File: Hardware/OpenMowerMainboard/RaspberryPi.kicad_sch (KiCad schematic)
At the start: 13 parts, among them J21 Raspberry_Pi_2_3, J22 Conn_02x04_Odd_Even, M1 Fan, Q3 BSS138, SW1 MK-11C04-G013, U3 SIP32509DT

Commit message: feat(bom): update LCSC codes
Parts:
- J21: LCSC (none) -> C2685119
- Q3: LCSC C360338 -> C3040446
- R1, R2, R4: LCSC (none) -> C17414
- R5: LCSC (none) -> C114523
- U3: LCSC (none) -> C335619
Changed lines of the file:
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@@
+      (effects (font (size 1.27 1.27)) hide)
+    )
+    (property "LCSC" "C17414" (id 7) (at 184.15 152.4 0)
       (effects (font (size 1.27 1.27)) hide)
     )
@@
       (effects (font (size 1.27 1.27)) hide)
     )
+    (property "LCSC" "C335619" (id 7) (at 166.37 17.78 0)
+      (effects (font (size 1.27 1.27)) hide)
+    )
     (pin "1")
     (pin "2")
@@
       (effects (font (size 1.27 1.27)) hide)
     )
+    (property "LCSC" "C114523" (id 7) (at 101.6 49.53 0)
+      (effects (font (size 1.27 1.27)) hide)
+    )
     (pin "1")
     (pin "2")
@@
       (effects (font (size 1.27 1.27)) (justify left) hide)
     )
-    (property "LCSC" "C360338" (id 4) (at 114.3 49.53 0)
+    (property "LCSC" "C3040446" (id 4) (at 114.3 49.53 0)
       (effects (font (size 1.27 1.27)) hide)
     )
@@
       (effects (font (size 1.27 1.27)) hide)
     )
+    (property "LCSC" "C17414" (id 7) (at 93.98 57.15 0)
+      (effects (font (size 1.27 1.27)) hide)
+    )
     (pin "1")
     (pin "2")
@@
     )
     (property "Stock_PN" "J-SMD-2x20-.1F" (id 6) (at 107.315 133.985 0)
+      (effects (font (size 1.27 1.27)) hide)
+    )
+    (property "LCSC" "C2685119" (id 7) (at 107.315 133.985 0)
       (effects (font (size 1.27 1.27)) hide)
     )
@@
       (effects (font (size 1.27 1.27)) hide)
     )
+    (property "LCSC" "C17414" (id 7) (at 184.15 130.175 0)
+      (effects (font (size 1.27 1.27)) hide)
+    )

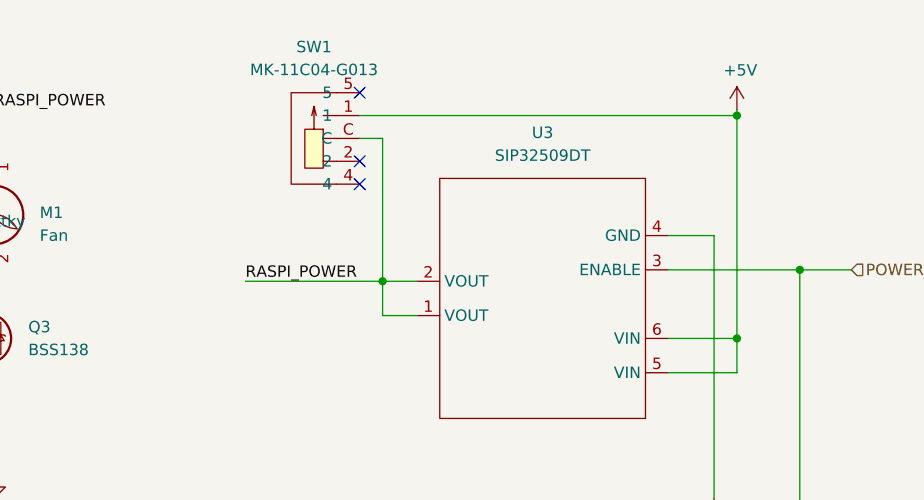
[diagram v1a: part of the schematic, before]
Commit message: feat(mb): add pin header for RPi force power
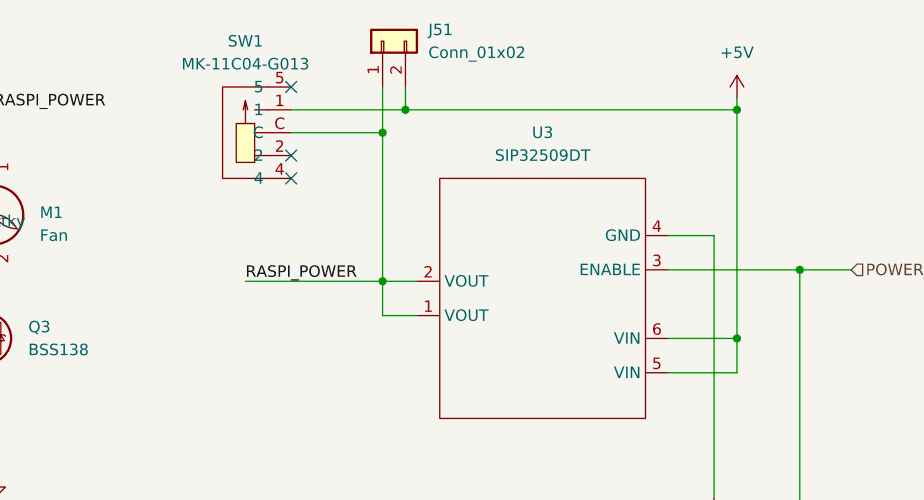
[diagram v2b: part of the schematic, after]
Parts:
- added J51: Conn_01x02, Connector_PinHeader_2.54mm:PinHeader_1x02_P2.54mm_Vertical, symbol Connector_Generic:Conn_01x02
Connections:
- net +5V: now also J51.2 (Pin_2)
- net RASPI_POWER: now also J51.1 (Pin_1)
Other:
- moved on the sheet: SW1
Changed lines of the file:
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@@
   (junction (at 107.315 171.45) (diameter 0) (color 0 0 0 0)
   )
+  (junction (at 162.56 24.13) (diameter 0) (color 0 0 0 0)
+  )
   (junction (at 114.935 171.45) (diameter 0) (color 0 0 0 0)
   )
@@
   (junction (at 116.84 43.18) (diameter 0) (color 0 0 0 0)
   )
-  (junction (at 199.39 24.765) (diameter 0) (color 0 0 0 0)
+  (junction (at 199.39 24.13) (diameter 0) (color 0 0 0 0)
   )
   (junction (at 102.235 171.45) (diameter 0) (color 0 0 0 0)
@@
   (junction (at 206.375 41.91) (diameter 0) (color 0 0 0 0)
   )
-  (no_connect (at 157.48 32.385))
-  (no_connect (at 157.48 29.845))
+  (junction (at 160.02 26.67) (diameter 0) (color 0 0 0 0)
+  )
+  (no_connect (at 149.86 31.75))
+  (no_connect (at 149.86 29.21))
   (no_connect (at 127.635 121.285))
   (no_connect (at 127.635 118.745))
@@
   (no_connect (at 127.635 146.685))
   (no_connect (at 127.635 136.525))
-  (no_connect (at 157.48 22.225))
+  (no_connect (at 149.86 21.59))
   (wire (pts (xy 158.115 111.125) (xy 127.635 111.125))
     (stroke (width 0) (type default) (color 0 0 0 0))
@@
     (stroke (width 0) (type default) (color 0 0 0 0))
   )
+  (wire (pts (xy 160.02 21.59) (xy 160.02 26.67))
+    (stroke (width 0) (type default) (color 0 0 0 0))
+  )
+  (wire (pts (xy 162.56 21.59) (xy 162.56 24.13))
+    (stroke (width 0) (type default) (color 0 0 0 0))
+  )
   (wire (pts (xy 127.635 144.145) (xy 184.15 144.145))
     (stroke (width 0) (type default) (color 0 0 0 0))
@@
     (stroke (width 0) (type default) (color 0 0 0 0))
   )
-  (wire (pts (xy 157.48 24.765) (xy 199.39 24.765))
+  (wire (pts (xy 149.86 24.13) (xy 162.56 24.13))
     (stroke (width 0) (type default) (color 0 0 0 0))
   )
@@
     (stroke (width 0) (type default) (color 0 0 0 0))
   )
-  (wire (pts (xy 157.48 27.305) (xy 160.02 27.305))
+  (wire (pts (xy 149.86 26.67) (xy 160.02 26.67))
     (stroke (width 0) (type default) (color 0 0 0 0))
   )
@@
     (stroke (width 0) (type default) (color 0 0 0 0))
   )
-  (wire (pts (xy 160.02 27.305) (xy 160.02 43.18))
-    (stroke (width 0) (type default) (color 0 0 0 0))
-  )
-  (wire (pts (xy 199.39 24.765) (xy 199.39 49.53))
+  (wire (pts (xy 199.39 24.13) (xy 199.39 49.53))
     (stroke (width 0) (type default) (color 0 0 0 0))
   )
@@
     (stroke (width 0) (type default) (color 0 0 0 0))
   )
+  (wire (pts (xy 162.56 24.13) (xy 199.39 24.13))
+    (stroke (width 0) (type default) (color 0 0 0 0))
+  )
   (wire (pts (xy 116.84 41.91) (xy 116.84 43.18))
     (stroke (width 0) (type default) (color 0 0 0 0))
@@
     (stroke (width 0) (type default) (color 0 0 0 0))
   )
-  (wire (pts (xy 199.39 24.13) (xy 199.39 24.765))
+  (wire (pts (xy 199.39 22.86) (xy 199.39 24.13))
     (stroke (width 0) (type default) (color 0 0 0 0))
   )
@@
   )
   (wire (pts (xy 55.245 130.175) (xy 49.53 130.175))
+    (stroke (width 0) (type default) (color 0 0 0 0))
+  )
+  (wire (pts (xy 160.02 26.67) (xy 160.02 43.18))
     (stroke (width 0) (type default) (color 0 0 0 0))
   )
@@
     (effects (font (size 1.27 1.27)) (justify right))
   )
-  (symbol (lib_id "power:+5V") (at 199.39 24.13 0) (unit 1)
-    (in_bom yes) (on_board yes)
-    (property "Reference" "#PWR0114" (id 0) (at 199.39 27.94 0)
-      (effects (font (size 1.27 1.27)) hide)
-    )
-    (property "Value" "+5V" (id 1) (at 199.771 19.7358 0))
-    (property "Footprint" "" (id 2) (at 199.39 24.13 0)
-      (effects (font (size 1.27 1.27)) hide)
-    )
-    (property "Datasheet" "" (id 3) (at 199.39 24.13 0)
+  (symbol (lib_id "power:+5V") (at 199.39 22.86 0) (unit 1)
+    (in_bom yes) (on_board yes) (fields_autoplaced)
+    (property "Reference" "#PWR0114" (id 0) (at 199.39 26.67 0)
+      (effects (font (size 1.27 1.27)) hide)
+    )
+    (property "Value" "+5V" (id 1) (at 199.39 17.78 0))
+    (property "Footprint" "" (id 2) (at 199.39 22.86 0)
+      (effects (font (size 1.27 1.27)) hide)
+    )
+    (property "Datasheet" "" (id 3) (at 199.39 22.86 0)
       (effects (font (size 1.27 1.27)) hide)
     )
@@
     )
     (property "Stock_PN" "J-TH-1x2-.1" (id 6) (at 116.84 36.83 0)
+      (effects (font (size 1.27 1.27)) hide)
+    )
+    (pin "1")
+    (pin "2")
+  )
+  (symbol (lib_id "Connector_Generic:Conn_01x02") (at 160.02 16.51 90) (unit 1)
+    (in_bom yes) (on_board yes) (fields_autoplaced)
+    (property "Reference" "J51" (id 0) (at 165.1 15.2399 90)
+      (effects (font (size 1.27 1.27)) (justify right))
+    )
+    (property "Value" "Conn_01x02" (id 1) (at 165.1 17.7799 90)
+      (effects (font (size 1.27 1.27)) (justify right))
+    )
+    (property "Footprint" "Connector_PinHeader_2.54mm:PinHeader_1x02_P2.54mm_Vertical" (id 2) (at 160.02 16.51 0)
+      (effects (font (size 1.27 1.27)) hide)
+    )
+    (property "Datasheet" "~" (id 3) (at 160.02 16.51 0)
       (effects (font (size 1.27 1.27)) hide)
     )
@@
     (pin "6")
   )
-  (symbol (lib_id "lcsc:MK-11C04-G013") (at 152.4 27.305 270) (unit 1)
-    (in_bom yes) (on_board yes) (fields_autoplaced)
-    (property "Reference" "SW1" (id 0) (at 152.4 17.145 90))
-    (property "Value" "MK-11C04-G013" (id 1) (at 152.4 19.685 90))
-    (property "Footprint" "lcsc:SW-SMD_MK-11C04-G013" (id 2) (at 149.86 27.305 0)
-      (effects (font (size 1.27 1.27)) hide)
-    )
-    (property "Datasheet" "https://lcsc.com/product-detail/Toggle-Switches_G-Switch-MK-11C04-G013_C778185.html" (id 3) (at 147.32 27.305 0)
-      (effects (font (size 1.27 1.27)) hide)
-    )
-    (property "Manufacturer" "G-Switch" (id 4) (at 144.78 27.305 0)
-      (effects (font (size 1.27 1.27)) hide)
-    )
-    (property "LCSC Part" "C778185" (id 5) (at 142.24 27.305 0)
-      (effects (font (size 1.27 1.27)) hide)
-    )
-    (property "JLC Part" "Extended Part" (id 6) (at 139.7 27.305 0)
-      (effects (font (size 1.27 1.27)) hide)
-    )
-    (property "LCSC" "C778185" (id 7) (at 152.4 27.305 0)
-      (effects (font (size 1.27 1.27)) hide)
-    )
+  (symbol (lib_id "lcsc:MK-11C04-G013") (at 144.78 26.67 270) (unit 1)
+    (in_bom yes) (on_board yes) (fields_autoplaced)
+    (property "Reference" "SW1" (id 0) (at 144.78 16.51 90))
+    (property "Value" "MK-11C04-G013" (id 1) (at 144.78 19.05 90))
+    (property "Footprint" "lcsc:SW-SMD_MK-11C04-G013" (id 2) (at 142.24 26.67 0)
+      (effects (font (size 1.27 1.27)) hide)
+    )
+    (property "Datasheet" "https://lcsc.com/product-detail/Toggle-Switches_G-Switch-MK-11C04-G013_C778185.html" (id 3) (at 139.7 26.67 0)
+      (effects (font (size 1.27 1.27)) hide)
+    )
+    (property "Manufacturer" "G-Switch" (id 4) (at 137.16 26.67 0)
+      (effects (font (size 1.27 1.27)) hide)
+    )
+    (property "LCSC Part" "C778185" (id 5) (at 134.62 26.67 0)
+      (effects (font (size 1.27 1.27)) hide)
+    )
+    (property "JLC Part" "Extended Part" (id 6) (at 132.08 26.67 0)
+      (effects (font (size 1.27 1.27)) hide)
+    )
+    (property "LCSC" "C778185" (id 7) (at 144.78 26.67 0)
+      (effects (font (size 1.27 1.27)) hide)
+    )

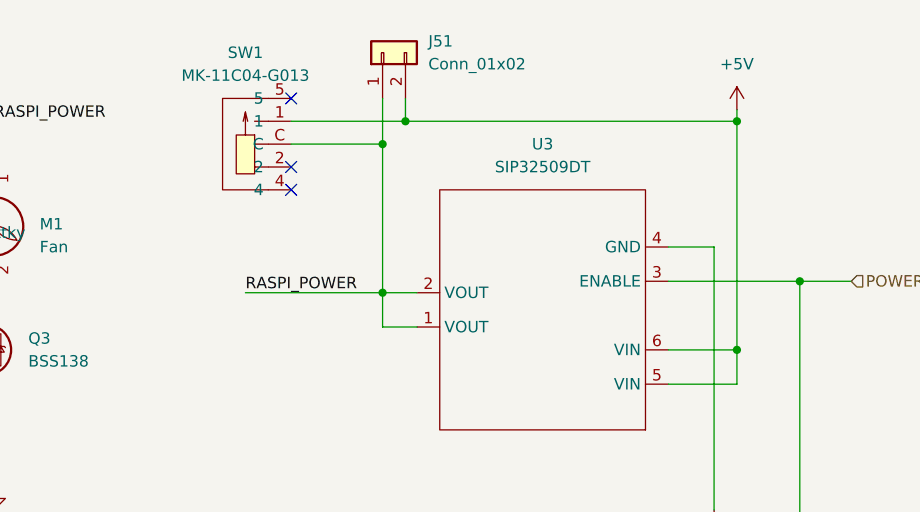
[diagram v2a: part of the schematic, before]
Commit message: feat(mb): replace SW1 with DIP variant, remove J51
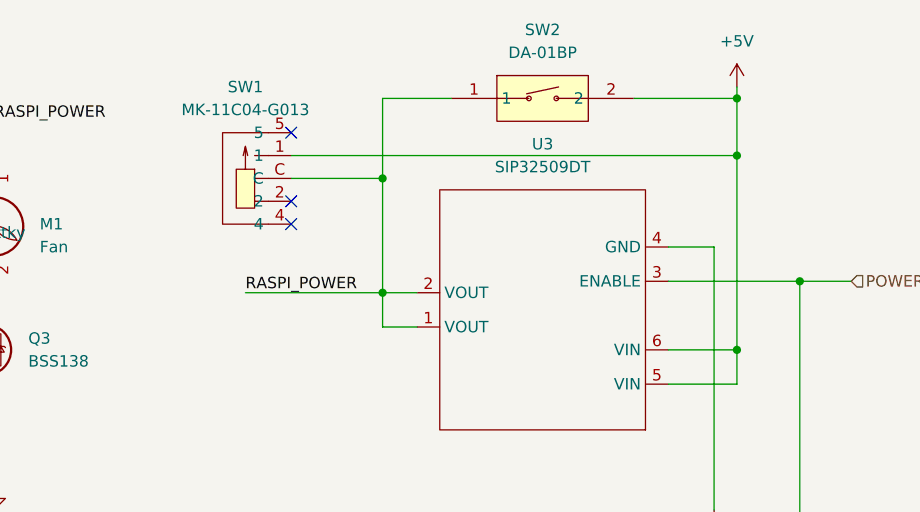
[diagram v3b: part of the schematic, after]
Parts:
- removed J51: Conn_01x02, Connector_PinHeader_2.54mm:PinHeader_1x02_P2.54mm_Vertical, symbol Connector_Generic:Conn_01x02
- added SW2: DA-01BP, lcsc:SW-TH_DA-01BP, symbol lcsc:DA-01BP
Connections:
- net +5V: now also SW2.2
- net RASPI_POWER: now also SW2.1
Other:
- moved on the sheet: SW1

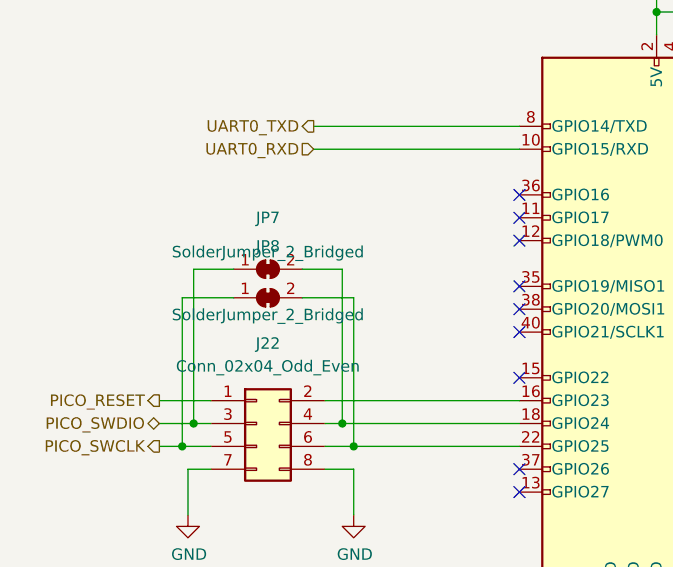
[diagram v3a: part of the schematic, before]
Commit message: feat: update to Kicad7, put back C2,C3
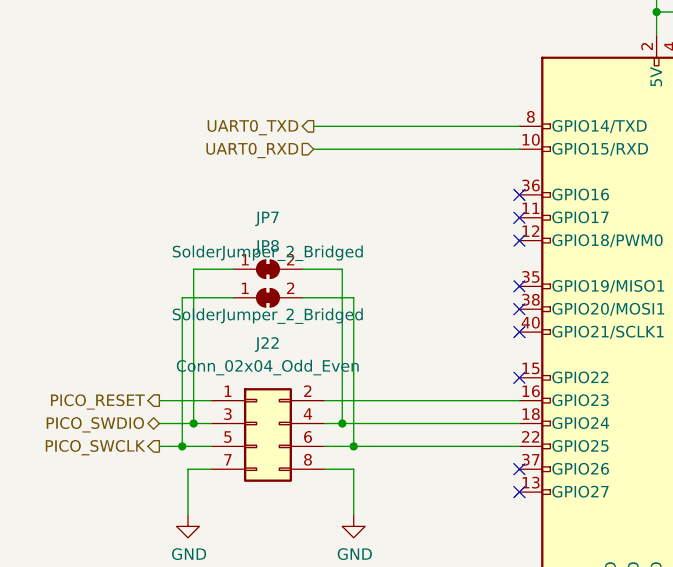
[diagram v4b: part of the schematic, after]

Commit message: upgraded to KiCAD v8
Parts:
- SW1: now left out of the parts list
